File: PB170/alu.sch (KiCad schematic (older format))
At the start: 0 parts

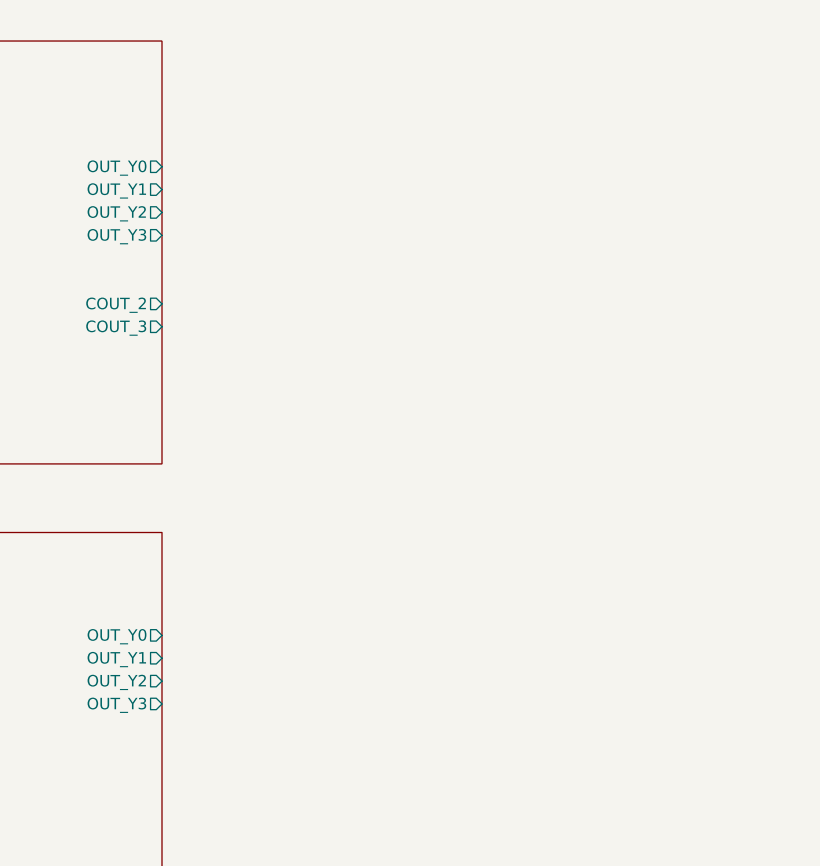
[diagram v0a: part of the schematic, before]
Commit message: Create operation multiplexer
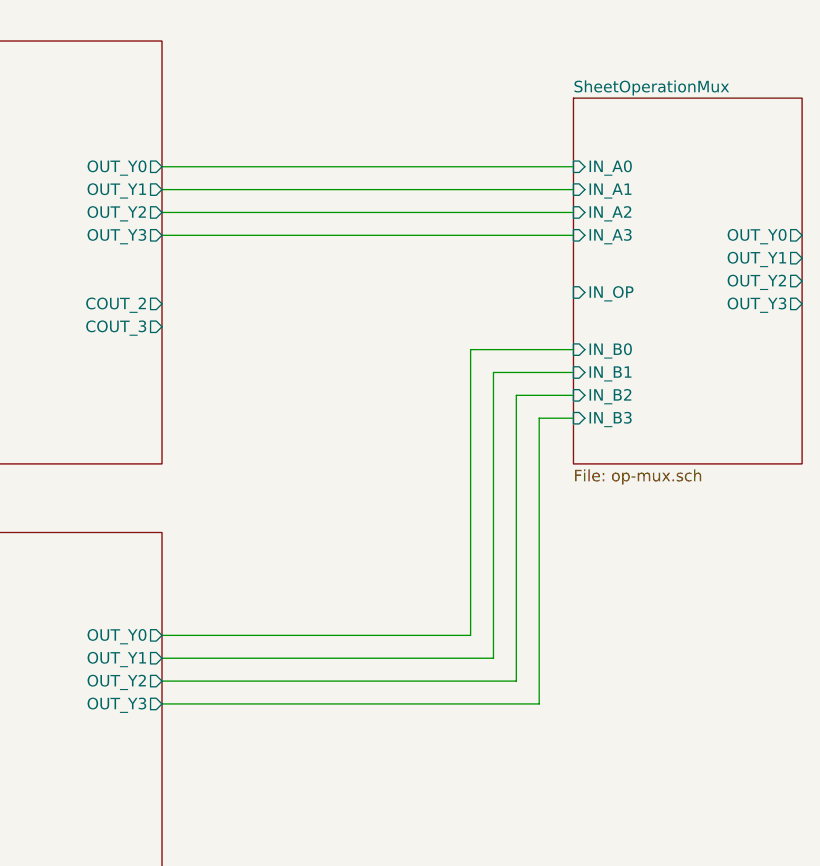
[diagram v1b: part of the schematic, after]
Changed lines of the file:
@@
 $Descr A4 11693 8268
 encoding utf-8
-Sheet 4 6
+Sheet 4 7
 Title ""
 Date ""
@@
 F14 "OUT_Y3" O R 4900 4450 50
 $EndSheet
+$Sheet
+S 6700 1800 1000 1600
+U 600D6CED
+F0 "SheetOperationMux" 50
+F1 "op-mux.sch" 50
+F2 "IN_A0" I L 6700 2100 50
+F3 "IN_A1" I L 6700 2200 50
+F4 "IN_A2" I L 6700 2300 50
+F5 "IN_A3" I L 6700 2400 50
+F6 "IN_B0" I L 6700 2900 50
+F7 "IN_B1" I L 6700 3000 50
+F8 "IN_B2" I L 6700 3100 50
+F9 "IN_B3" I L 6700 3200 50
+F10 "IN_OP" I L 6700 2650 50
+F11 "OUT_Y0" O R 7700 2400 50
+F12 "OUT_Y1" O R 7700 2500 50
+F13 "OUT_Y2" O R 7700 2600 50
+F14 "OUT_Y3" O R 7700 2700 50
+$EndSheet
+Wire Wire Line
+	4900 2100 6700 2100
+Wire Wire Line
+	4900 2200 6700 2200
+Wire Wire Line
+	4900 2300 6700 2300
+Wire Wire Line
+	4900 2400 6700 2400
+Wire Wire Line
+	4900 4450 6550 4450
+Wire Wire Line
+	6550 4450 6550 3200
+Wire Wire Line
+	6550 3200 6700 3200
+Wire Wire Line
+	4900 4350 6450 4350
+Wire Wire Line
+	6450 4350 6450 3100
+Wire Wire Line
+	6450 3100 6700 3100
+Wire Wire Line
+	4900 4250 6350 4250
+Wire Wire Line
+	6350 4250 6350 3000
+Wire Wire Line
+	6350 3000 6700 3000
+Wire Wire Line
+	4900 4150 6250 4150
+Wire Wire Line
+	6250 4150 6250 2900
+Wire Wire Line
+	6250 2900 6700 2900
 $EndSCHEMATC

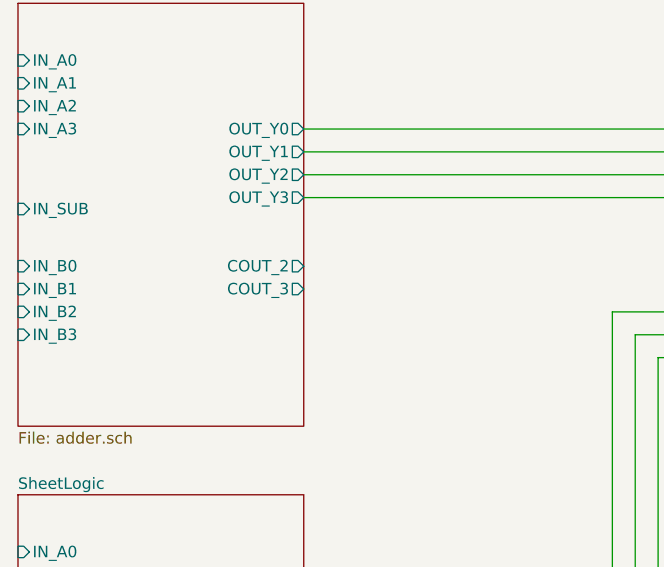
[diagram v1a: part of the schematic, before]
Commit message: Create overlow label in adder
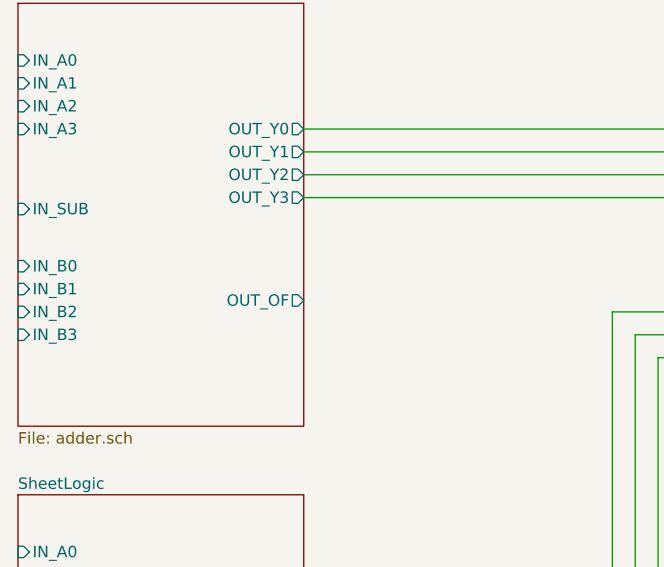
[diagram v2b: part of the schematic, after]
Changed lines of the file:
@@
 F13 "OUT_Y2" O R 4900 2300 50
 F14 "OUT_Y3" O R 4900 2400 50
-F15 "COUT_3" O R 4900 2800 50
-F16 "COUT_2" O R 4900 2700 50
+F15 "OUT_OF" O R 4900 2850 50
 $EndSheet
 $Sheet

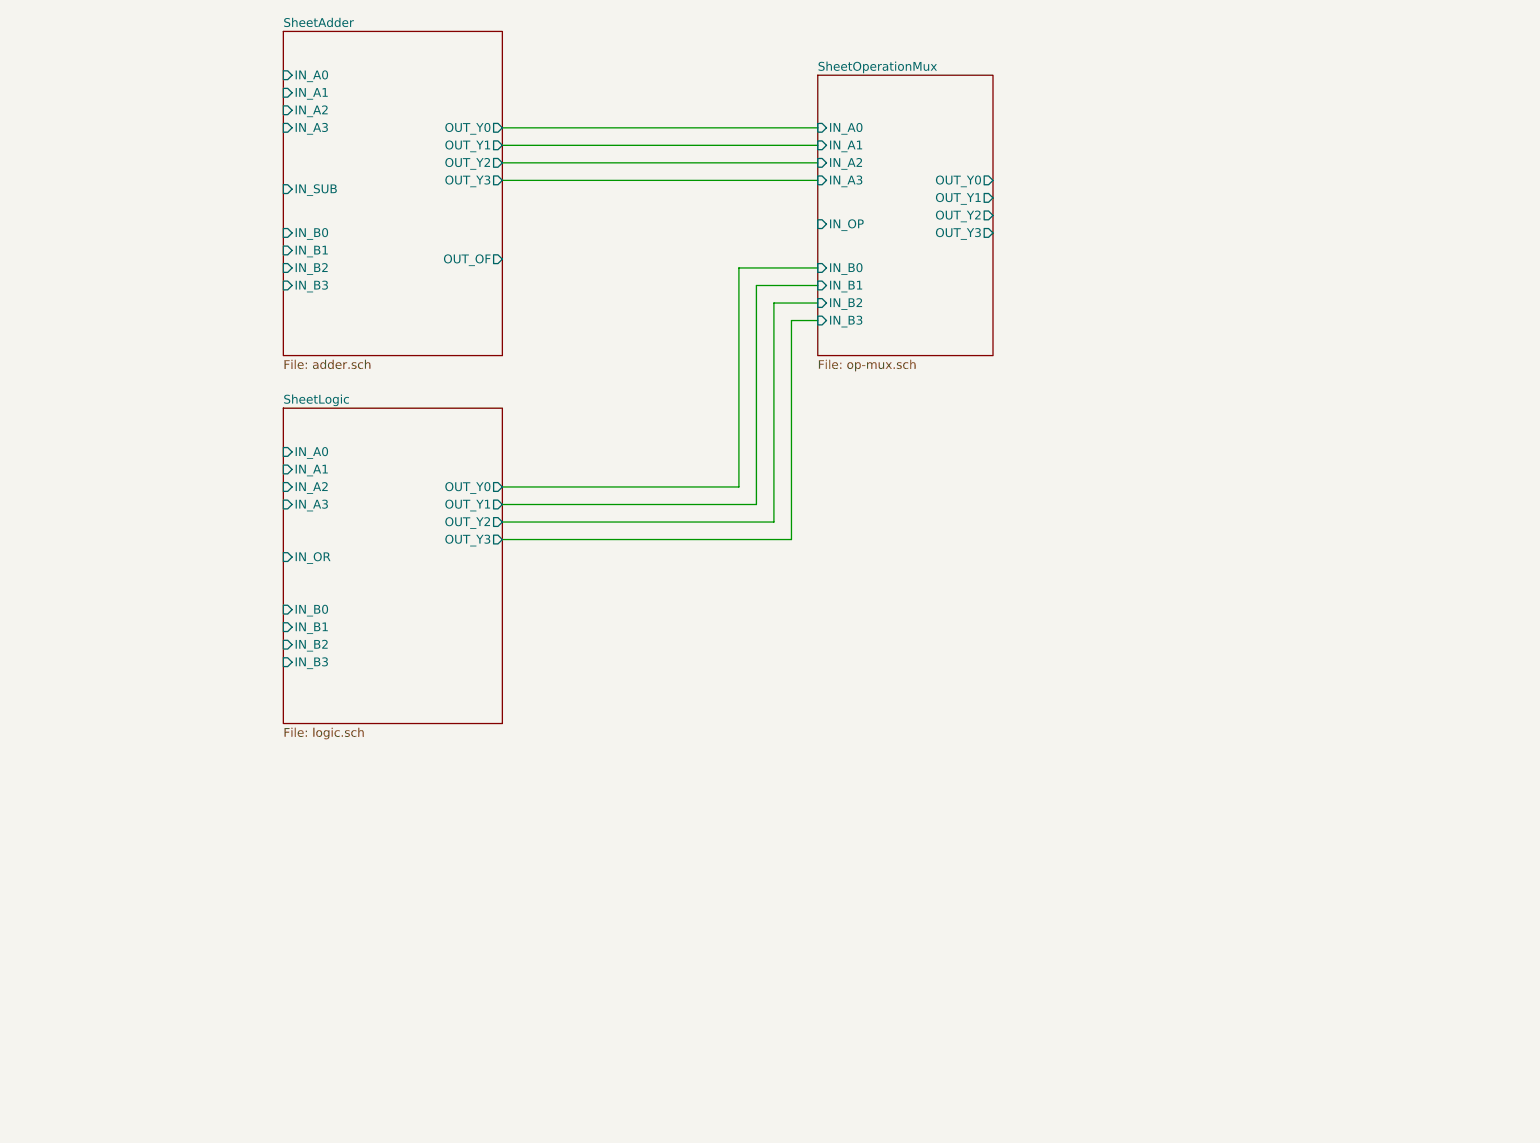
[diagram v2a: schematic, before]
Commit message: Add alu output flags
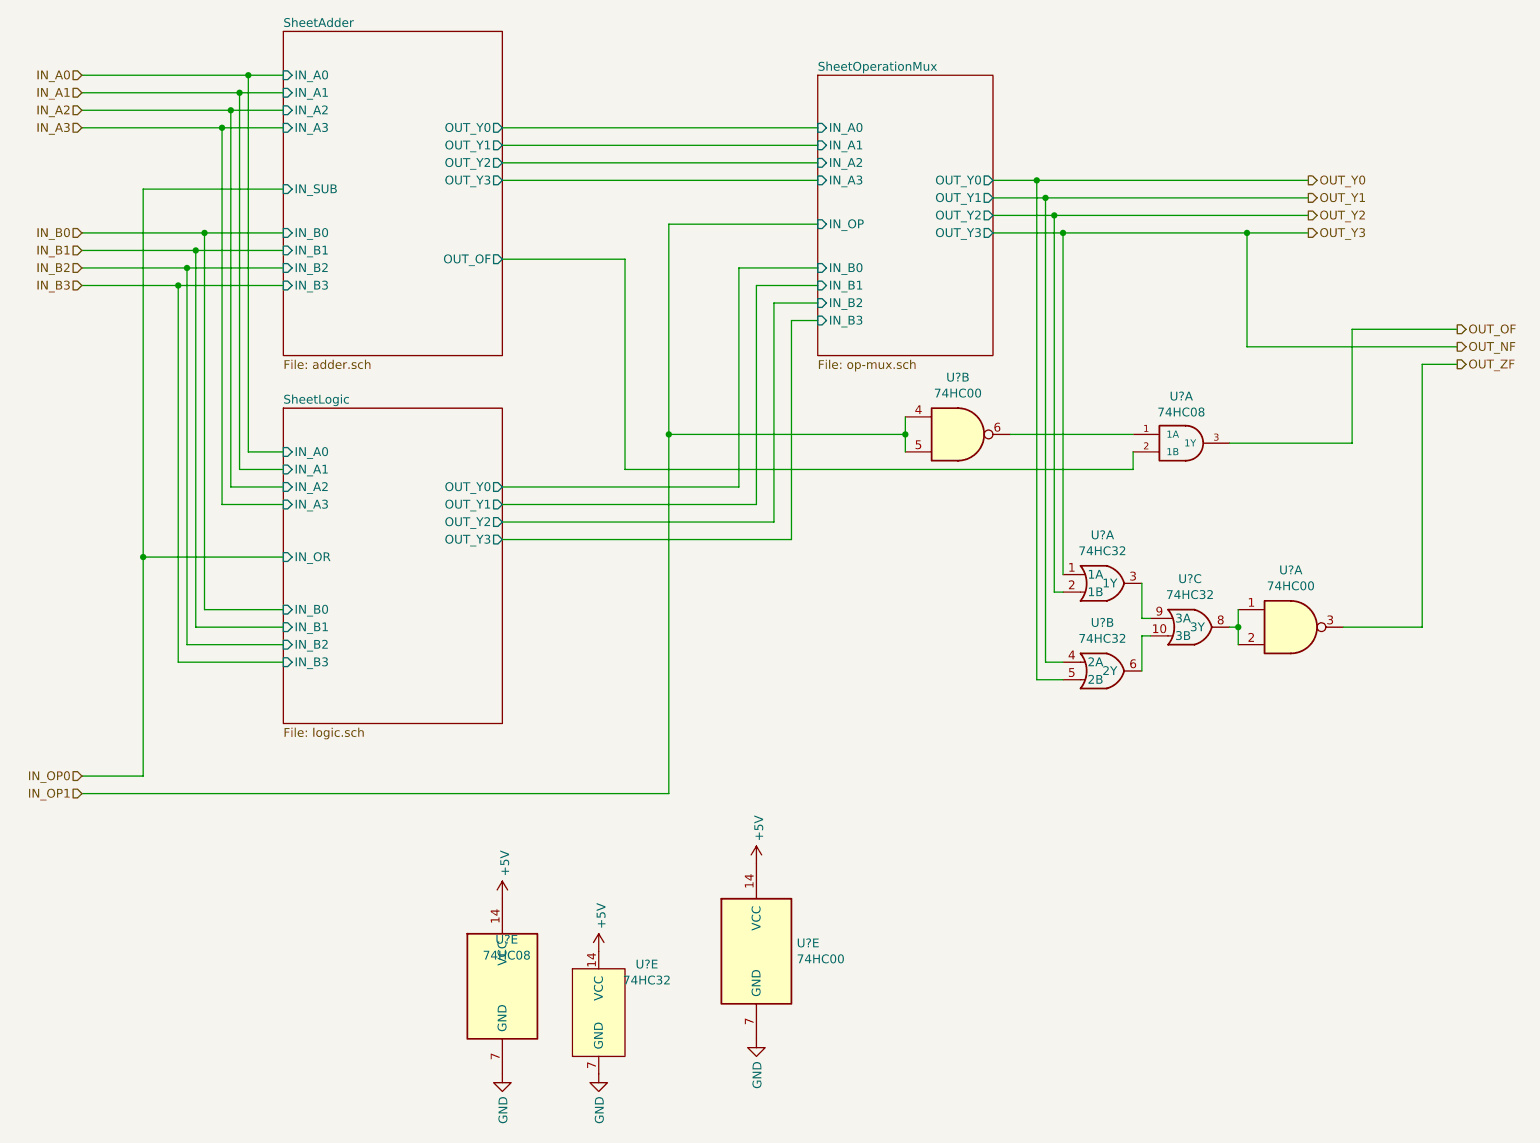
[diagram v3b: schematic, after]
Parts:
- added U? (x4): 74HC32, Housings_SOIC:SOIC-14_3.9x8.7mm_Pitch1.27mm, symbol PB170:74HC32
- added U? (x3): 74HC00, Package_SO:TSSOP-14_4.4x5mm_P0.65mm, symbol 74xx:74HC00
- added U? (x2): 74HC08, Housings_SOIC:SOIC-14_3.9x8.7mm_Pitch1.27mm, symbol PB170:74HC08
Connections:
- net SheetAdder/OUT_OF: now also U?.2 (1B)
- new net: U?.3 (1Y), U?.9 (3A)
- new net: U?.10 (3B), U?.6 (2Y)
- new net: U?.1, U?.2, U?.8 (3Y)
- new net: U?.1 (1A), U?.6
- new net +5V: U?.14 (VCC), U?.14 (VCC), U?.14 (VCC)
- new net GND: U?.7 (GND), U?.7 (GND), U?.7 (GND)
- new net IN_OP1: U?.4, U?.5
- new net OUT_NF: U?.1 (1A)
- new net OUT_OF: U?.3 (1Y)
- new net OUT_Y0: U?.5 (2B)
- new net OUT_Y1: U?.4 (2A)
- new net OUT_Y2: U?.2 (1B)
- new net OUT_ZF: U?.3

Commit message: ALU finished
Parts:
- added U?: 74HC00, symbol 74xx:74HC00
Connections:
- net IN_OP0: now also U?.10, U?.9
- net SheetAdder/OUT_OF: now also U?.1 (1A); no longer U?.2 (1B)
- net SheetOperationMux/IN_NOT_OP: now reaches U?.6
- net SheetOperationMux/IN_NOT_OP: now also U?.2 (1B); no longer U?.1 (1A)
- new net SheetLogic/IN_NOT_OR: U?.8
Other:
- moved on the sheet: U?B
